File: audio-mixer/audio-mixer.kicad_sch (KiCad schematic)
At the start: 63 parts, among them J1 Input A1, J10 Output A, J11 Output B, J12 Conn_01x11_Socket, J13 AudioJack4, J14 Input A1, J15 Input B1, J16 Input A2, J17 Input B2, J18 Input A3, J19 Input B3, J2 Power, J20 Output A, J21 Output B, J22 Conn_01x11_Pin, J23 Conn_01x03_Pin, J3 Power, J4 Power, J5 Input B1, J6 Input A2, J7 Input B2, J8 Input A3, J9 Input B3, SW1 Iso A1, SW2 Iso B1, SW3 Iso A2, SW4 Iso B2, SW5 Iso A3, SW6 Iso B3, SW7 Iso A, SW8 Iso B, SW9 Mono/Stereo, U1 TL074

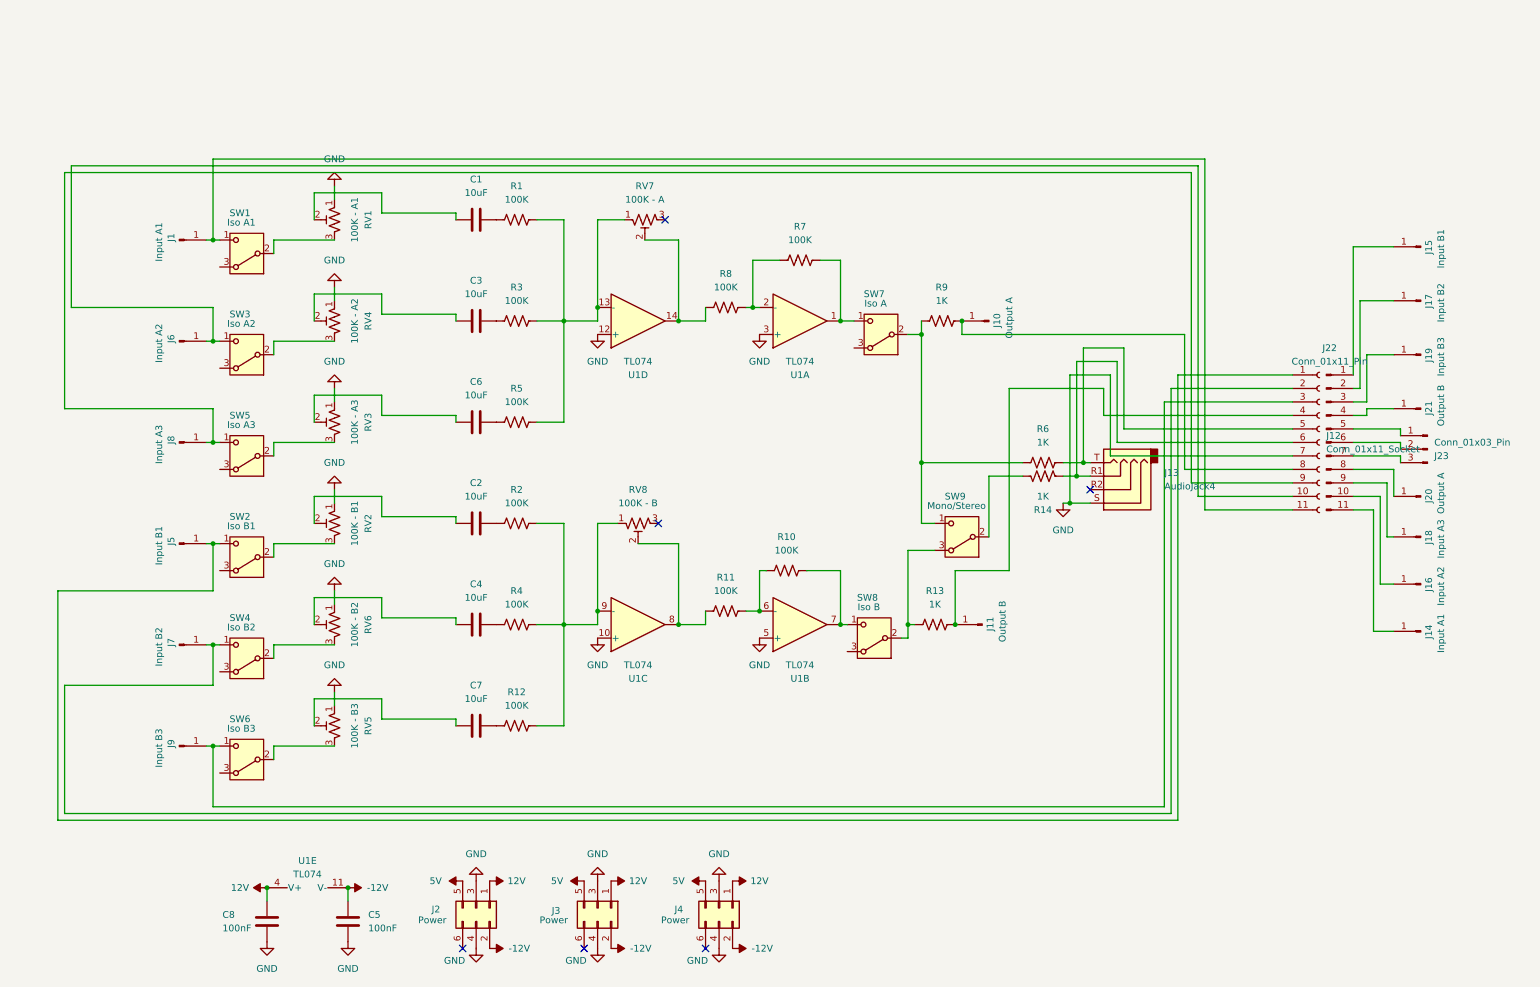
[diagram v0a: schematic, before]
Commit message: Extra channels in audio mixer
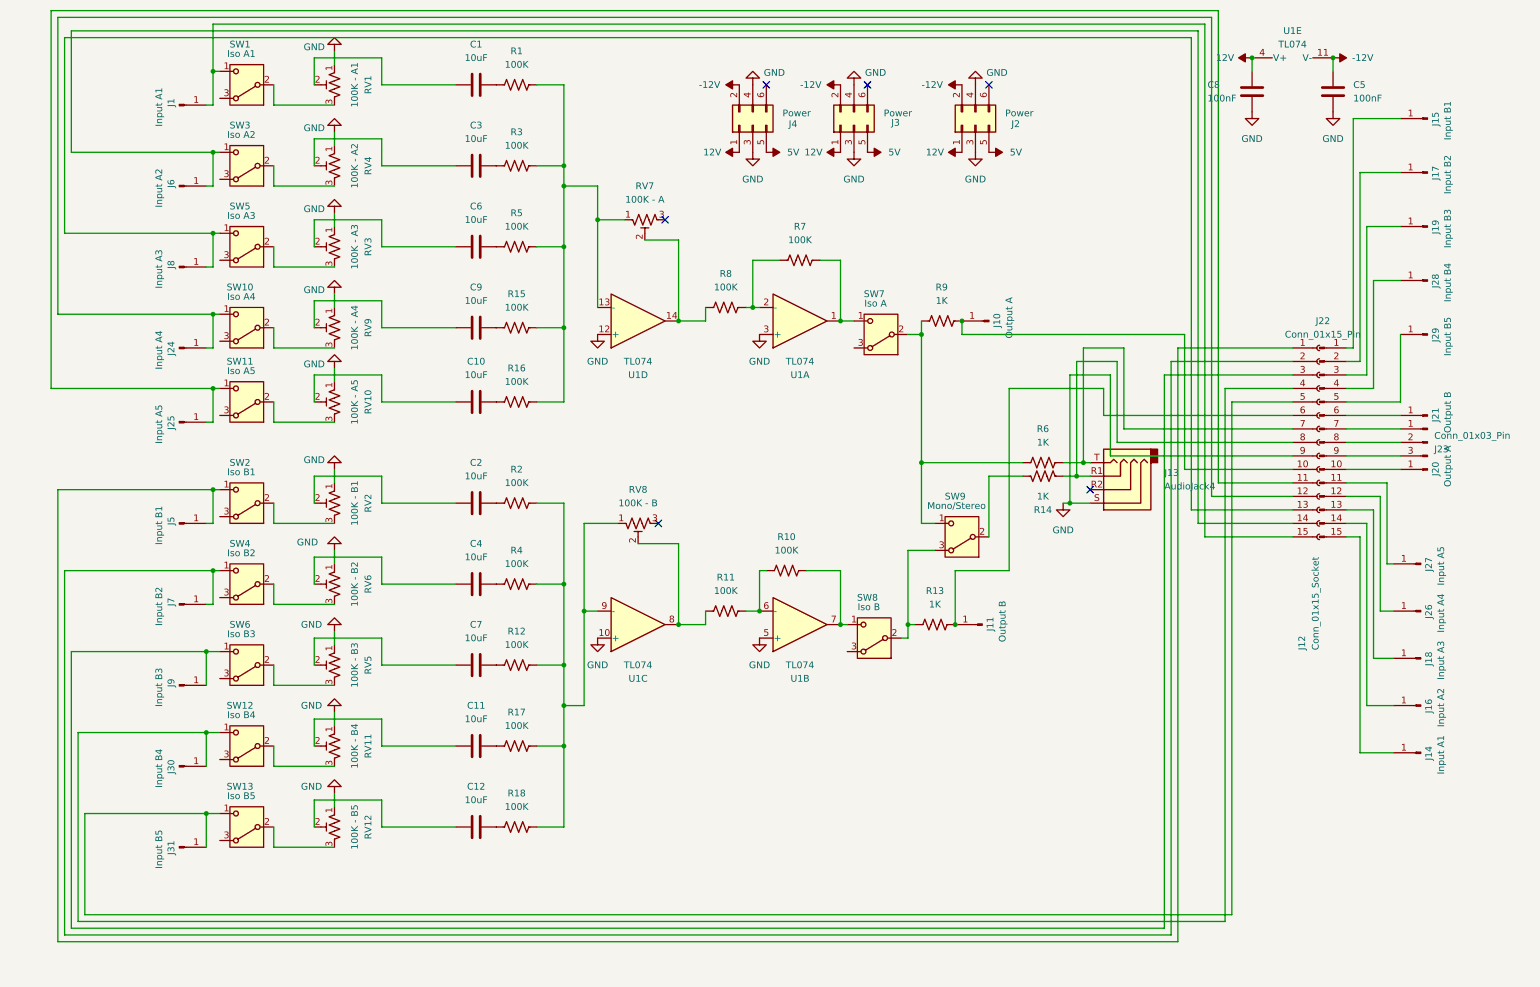
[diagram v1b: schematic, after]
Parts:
- removed J12: Conn_01x11_Socket, Connector_PinSocket_2.54mm:PinSocket_1x11_P2.54mm_Vertical, symbol Connector:Conn_01x11_Socket
- removed J22: Conn_01x11_Pin, Connector_PinHeader_2.54mm:PinHeader_1x11_P2.54mm_Vertical, symbol Connector:Conn_01x11_Pin
- added C10, C11, C12, C9: 10uF, Capacitor_THT:C_Disc_D4.3mm_W1.9mm_P5.00mm, symbol Device:C
- added J12: Conn_01x15_Socket, Connector_PinSocket_2.54mm:PinSocket_1x15_P2.54mm_Vertical, symbol Connector:Conn_01x15_Socket
- added J22: Conn_01x15_Pin, Connector_PinHeader_2.54mm:PinHeader_1x15_P2.54mm_Vertical, symbol Connector:Conn_01x15_Pin
- added J24, J26: Input A4, modular2:banana-jack, symbol Connector:Conn_01x01_Pin
- added J25, J27: Input A5, modular2:banana-jack, symbol Connector:Conn_01x01_Pin
- added J28, J30: Input B4, modular2:banana-jack, symbol Connector:Conn_01x01_Pin
- added J29, J31: Input B5, modular2:banana-jack, symbol Connector:Conn_01x01_Pin
- added R15, R16, R17, R18: 100K, Resistor_THT:R_Axial_DIN0207_L6.3mm_D2.5mm_P10.16mm_Horizontal, symbol Device:R_US
- added RV10: 100K - A5, modular2:Potentiometer_Alps_RK09K_Single_Vertical - knob padding, symbol Device:R_Potentiometer_Trim_US
- added RV11: 100K - B4, modular2:Potentiometer_Alps_RK09K_Single_Vertical - knob padding, symbol Device:R_Potentiometer_Trim_US
- added RV12: 100K - B5, modular2:Potentiometer_Alps_RK09K_Single_Vertical - knob padding, symbol Device:R_Potentiometer_Trim_US
- added RV9: 100K - A4, modular2:Potentiometer_Alps_RK09K_Single_Vertical - knob padding, symbol Device:R_Potentiometer_Trim_US
- added SW10: Iso A4, modular2:switch1, symbol Switch:SW_Nidec_CAS-120A1
- added SW11: Iso A5, modular2:switch1, symbol Switch:SW_Nidec_CAS-120A1
- added SW12: Iso B4, modular2:switch1, symbol Switch:SW_Nidec_CAS-120A1
- added SW13: Iso B5, modular2:switch1, symbol Switch:SW_Nidec_CAS-120A1
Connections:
- net GND: now also J12.9 (Pin_9), RV10.1, RV11.1, RV12.1, RV9.1
- net at J14.1 (Pin_1): now also J22.15 (Pin_15)
- net at R1.2, R3.2, R5.2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: now also R15.2, R16.2
- net at J9.1 (Pin_1), SW6.1 (C): now also J12.3 (Pin_3)
- net at J23.1 (Pin_1): now also J22.7 (Pin_7)
- net at J23.2 (Pin_2): now also J22.8 (Pin_8)
- net at J23.3 (Pin_3): now also J22.9 (Pin_9)
- net at J8.1 (Pin_1), SW5.1 (C): now also J12.13 (Pin_13)
- net at J5.1 (Pin_1), SW2.1 (C): now also J12.1 (Pin_1)
- net at J7.1 (Pin_1), SW4.1 (C): now also J12.2 (Pin_2)
- net at J6.1 (Pin_1), SW3.1 (C): now also J12.14 (Pin_14)
- net at J1.1 (Pin_1), SW1.1 (C): now also J12.15 (Pin_15)
- net at J15.1 (Pin_1): now also J22.1 (Pin_1)
- net at J16.1 (Pin_1): now also J22.14 (Pin_14)
- net at J17.1 (Pin_1): now also J22.2 (Pin_2)
- net at J19.1 (Pin_1): now also J22.3 (Pin_3)
- net at J21.1 (Pin_1): now also J22.6 (Pin_6)
- net at J20.1 (Pin_1): now also J22.10 (Pin_10)
- net at J18.1 (Pin_1): now also J22.13 (Pin_13)
- net at J10.1 (Pin_1), R9.2: now also J12.10 (Pin_10)
- net at J13.R1, R14.2: now also J12.8 (Pin_8)
- net at J13.T, R6.2: now also J12.7 (Pin_7)
- net at R12.2, R2.2, R4.2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: now also R17.2, R18.2
- net at J11.1 (Pin_1), R13.2: now also J12.6 (Pin_6)
- new net: C10.1, RV10.2
- new net: C10.2, R16.1
- new net: RV10.3, SW11.2 (B)
- new net: J12.11 (Pin_11), J25.1 (Pin_1), SW11.1 (C)
- new net: J12.12 (Pin_12), J24.1 (Pin_1), SW10.1 (C)
- new net: J12.4 (Pin_4), J30.1 (Pin_1), SW12.1 (C)
- new net: J12.5 (Pin_5), J31.1 (Pin_1), SW13.1 (C)
- new net: C12.1, RV12.2
- new net: C12.2, R18.1
- new net: C11.1, RV11.2
- new net: C11.2, R17.1
- new net: J22.11 (Pin_11), J27.1 (Pin_1)
- new net: J22.12 (Pin_12), J26.1 (Pin_1)
- new net: J22.4 (Pin_4), J28.1 (Pin_1)
- new net: J22.5 (Pin_5), J29.1 (Pin_1)
- new net: RV11.3, SW12.2 (B)
- new net: RV12.3, SW13.2 (B)
- new net: RV9.3, SW10.2 (B)
- new net: C9.1, RV9.2
- new net: C9.2, R15.1
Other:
- moved on the sheet: C1, C2, C3, C4, C5, C6, C7, C8, J1, J14, J15, J16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

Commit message: Update some pdfs
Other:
- moved on the sheet: C1, C10, C11, C12, C2, C3, C4, C5, C6, C7, C8, C9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
